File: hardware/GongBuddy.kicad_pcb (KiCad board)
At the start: 2 copper layers, 54 x 77 mm, 49 parts, among them J1 USB_B_Mini, J2 Conn_01x05, J3 2908-05WB-MG, J4 Conn_01x04, J5 Conn_01x02, J6 Conn_01x06, J7 Conn_Coaxial, J8 Conn_01x15, Q1 MMBT3904, U1 TPS7A19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

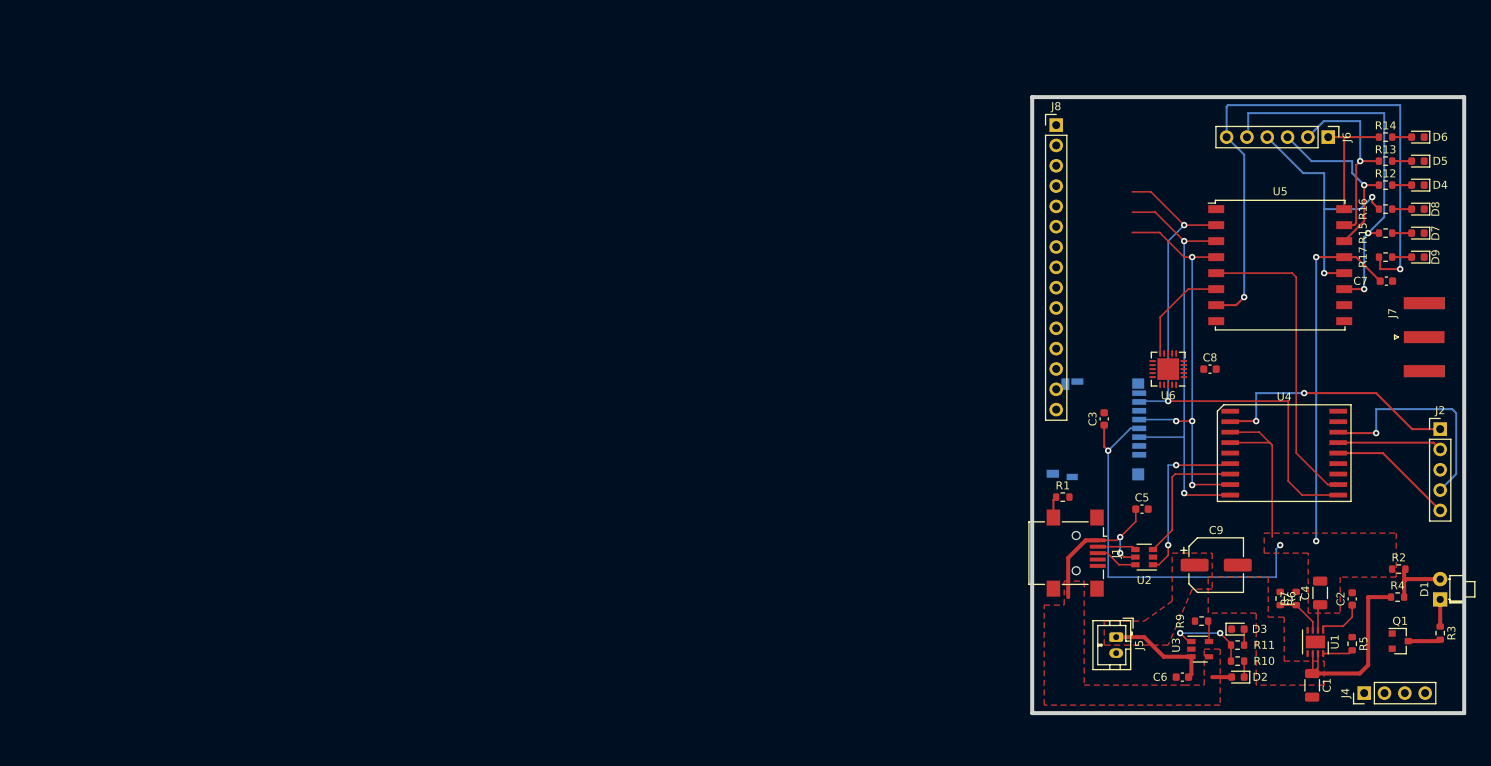
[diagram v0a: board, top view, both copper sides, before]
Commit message: Finished the layout and routing.
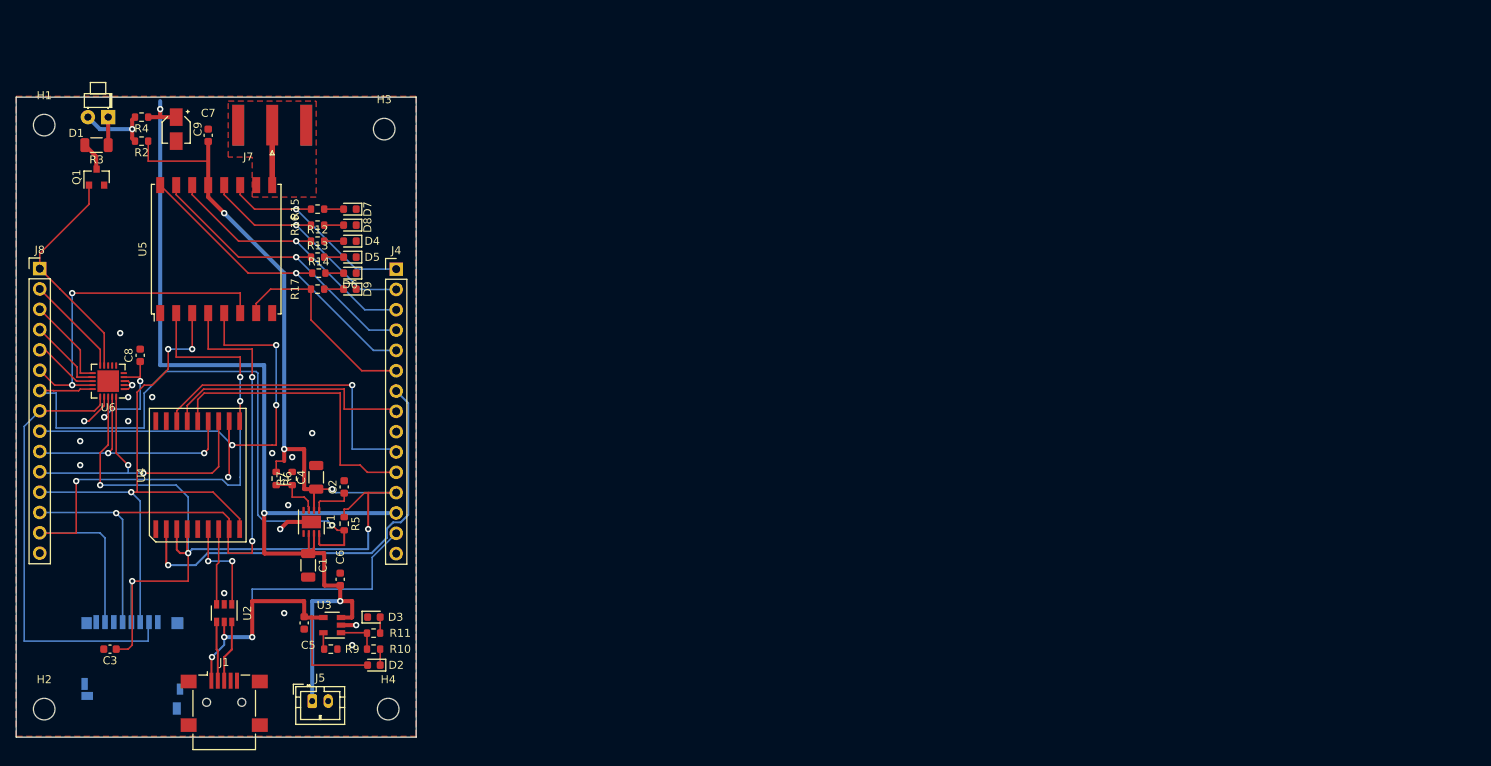
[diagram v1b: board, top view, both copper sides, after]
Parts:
- removed J2: Conn_01x05, Connector_PinHeader_2.54mm:PinHeader_1x05_P2.54mm_Vertical
- removed J6: Conn_01x06, Connector_PinHeader_2.54mm:PinHeader_1x06_P2.54mm_Vertical
- removed R1: 0, Resistor_SMD:R_0603_1608Metric
- added H1: MountingHole, MountingHole:MountingHole_2.7mm_M2.5, F.Cu at (33.5, 63.5)
- added H2: MountingHole, MountingHole:MountingHole_2.7mm_M2.5, F.Cu at (33.5, 136.5)
- added H3: MountingHole, MountingHole:MountingHole_2.7mm_M2.5, F.Cu at (76.0, 64.0)
- added H4: MountingHole, MountingHole:MountingHole_2.7mm_M2.5, F.Cu at (76.5, 136.5)
- C9: footprint Capacitor_SMD:CP_Elec_6.3x5.7 -> Capacitor_SMD:CP_Elec_3x5.3
- J4: value Conn_01x04 -> Conn_01x15; footprint Connector_PinHeader_2.54mm:PinHeader_1x04_P2.54mm_Vertical -> Connector_PinHeader_2.54mm:PinHeader_1x15_P2.54mm_Vertical
- R3: footprint Resistor_SMD:R_0603_1608Metric -> Resistor_SMD:R_1206_3216Metric
- moved R3 178.7 mm to (40.0, 66.0), turned to 180 degrees
- moved D1 177.1 mm to (41.5, 62.5), turned to 180 degrees
- moved Q1 173.0 mm to (40.0, 70.0), turned to 90 degrees
- moved R4 168.1 mm to (45.7, 62.5), turned to 180 degrees
- moved R2 166.0 mm to (45.7, 65.5), turned to 180 degrees
- moved C7 148.4 mm to (54.0, 64.8), turned to 90 degrees
- moved J7 146.4 mm to (62.0, 63.5), turned to 90 degrees
- moved C9 141.0 mm to (50.0, 64.0), turned to 270 degrees
- moved U4 135.8 mm to (52.7, 107.2), turned to 0 degrees
- moved D6 134.6 mm to (71.7, 82.0)
- moved R14 134.4 mm to (67.8, 82.0)
- moved D5 134.0 mm to (71.7, 80.0)
- moved R13 134.0 mm to (67.7, 80.0)
- moved C8 133.7 mm to (45.5, 92.3), turned to 90 degrees
- moved D4 133.7 mm to (71.7, 78.0)
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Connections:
- J1 pad 6: Net-(J1-Pad6) -> GND
- J4 pad 1: VCC -> /DIO3
- J4 pad 2: /VBAT -> /DIO4
- J4 pad 3: VBUS -> /DIO0
- J4 pad 4: GND -> /DIO1
- J8 pad 1: /SD_CS -> /BIG_LED
- J8 pad 10: /I2C_SDA -> /I2C_SCL
- J8 pad 11: /LORA_CS -> /I2C_SDA
- J8 pad 12: Net-(J8-Pad12) -> /SPI_MOSI
- J8 pad 14: /SPI_MOSI -> /SPI_MISO
- J8 pad 15: /SPI_MISO -> GND
- J8 pad 2: /LORA_RESET -> Net-(J8-Pad2)
- J8 pad 3: /BIG_LED -> Net-(J8-Pad3)
- J8 pad 4: /PG -> Net-(J8-Pad4)
- J8 pad 6: Net-(J8-Pad6) -> /LORA_RESET
- J8 pad 7: Net-(J8-Pad7) -> /PG
- J8 pad 8: Net-(J8-Pad8) -> /SD_CS
- J8 pad 9: /I2C_SCL -> /LORA_CS
- U6 pad 10: /LORA_RESET -> Net-(J8-Pad2)
- U6 pad 11: /BIG_LED -> Net-(J8-Pad3)
- U6 pad 12: /PG -> Net-(J8-Pad4)
- U6 pad 14: Net-(J8-Pad6) -> /LORA_RESET
- U6 pad 15: Net-(J8-Pad7) -> /PG
- U6 pad 16: Net-(J8-Pad8) -> /SD_CS
- U6 pad 9: /SD_CS -> /BIG_LED
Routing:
- net /VBAT: track 37.2 -> 132.3 mm, vias 0 -> 3
- net /PG: track 3.97 -> 79.7 mm, vias 0 -> 1
- net VCC: track 120.0 -> 195.4 mm, vias 4 -> 9
- net /SD_CS: track 0.00 -> 56.4 mm
- net /DIO5: track 75.0 -> 25.9 mm, vias 2 -> 0
- net VBUS: track 23.3 -> 69.0 mm, vias 2 -> 3
- net /I2C_SDA: track 0.00 -> 38.7 mm, vias 0 -> 2
- net /I2C_SCL: track 0.00 -> 32.1 mm, vias 0 -> 2
- net /LORA_RESET: track 13.0 -> 42.4 mm, vias 0 -> 2
- net /SPI_CLK: track 51.8 -> 80.9 mm, vias 4 -> 3
- net /BIG_LED: track 0.00 -> 28.4 mm
- net /DIO2: track 15.3 -> 40.1 mm, vias 0 -> 1
- net /LORA_CS: track 39.1 -> 63.5 mm, vias 0 -> 4
- net /VDD_OUT: track 31.6 -> 54.0 mm, vias 2 -> 1
- net /NRST: track 15.7 -> 37.2 mm
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- added copper zone on B.Cu, net GND
- added copper zone on F.Cu, net GND
- removed copper zone on F.Cu, net /VBAT
- removed copper zone on F.Cu, net VBUS
- removed copper zone on F.Cu, net VCC
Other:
- board size 54 x 77 mm -> 50 x 80 mm

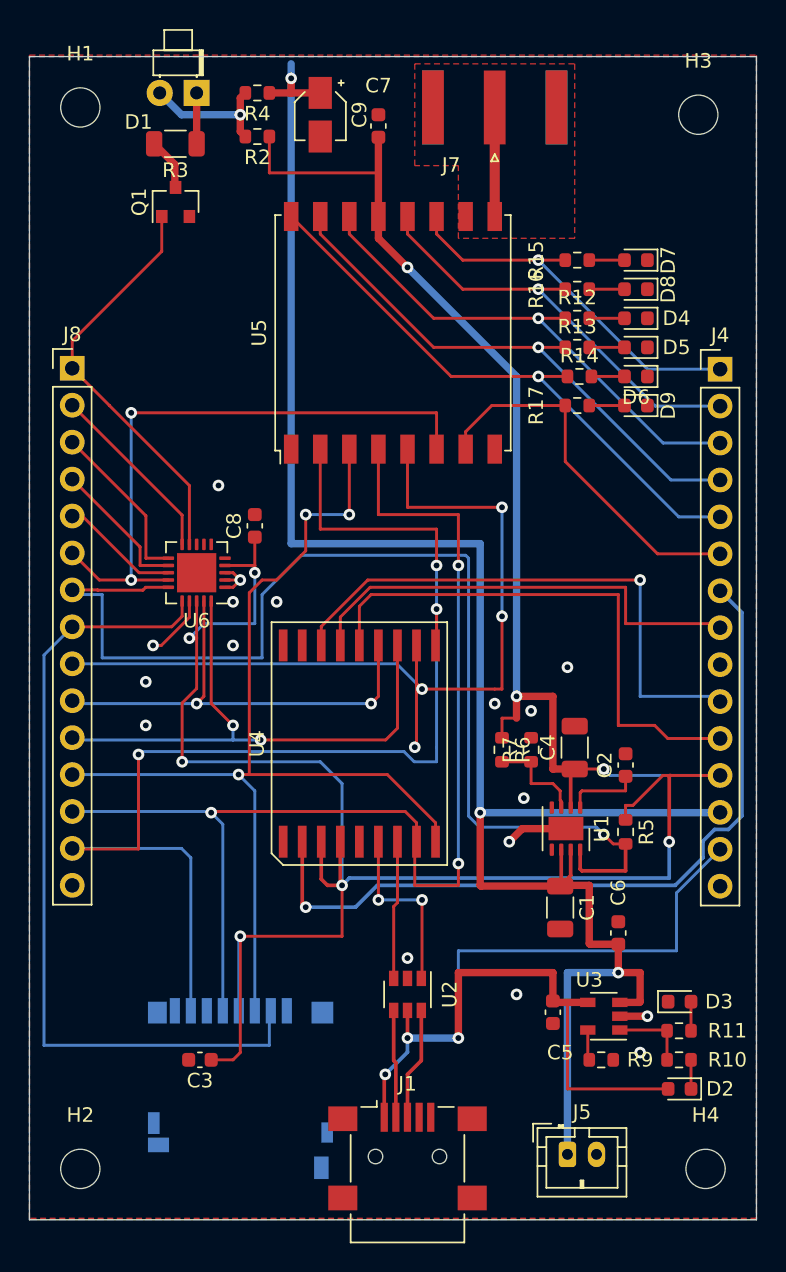
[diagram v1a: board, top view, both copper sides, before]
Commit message: Tweaked the layout slightly.
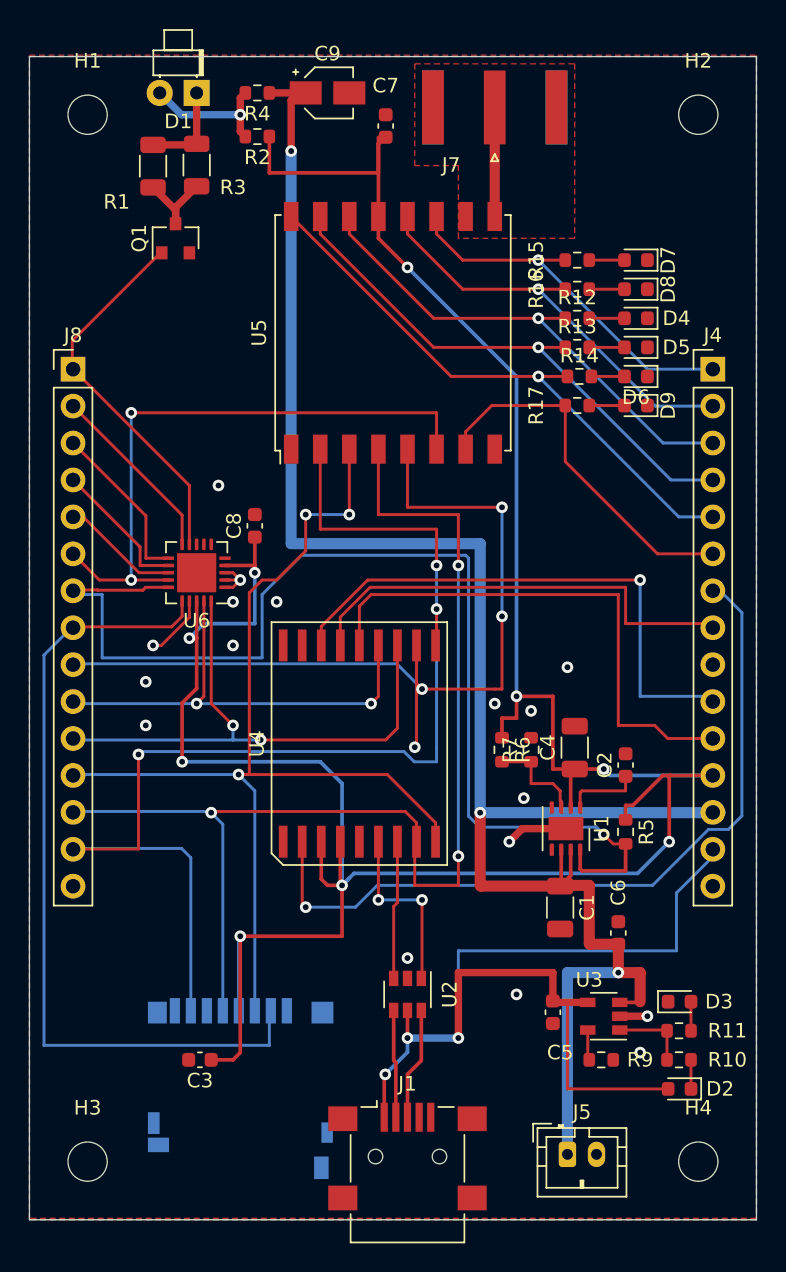
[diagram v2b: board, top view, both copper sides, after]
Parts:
- added R1: 50, Resistor_SMD:R_1206_3216Metric, F.Cu at (38.5, 67.5)
- moved H2 84.0 mm to (76.0, 64.0)
- moved H3 83.4 mm to (34.0, 136.0)
- moved Q1 2.50 mm to (40.0, 72.5)
- moved R3 2.07 mm to (41.5, 67.5), turned to 270 degrees
- moved C9 1.58 mm to (50.5, 62.5), turned to 0 degrees
- moved H1 0.71 mm to (34.0, 64.0)
- moved H4 0.71 mm to (76.0, 136.0)
- moved C7 0.50 mm to (54.5, 64.8)
- moved J4 0.50 mm to (77.0, 81.5)
- moved J8 0.08 mm to (33.0, 81.5)
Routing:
- net Net-(D1-Pad1): track 3.71 -> 6.74 mm
- net Net-(Q1-Pad3): track 3.61 -> 6.32 mm
- net /VBAT: track 132.3 -> 129.7 mm
- net /BIG_LED: track 28.4 -> 26.0 mm
- net /VDD_OUT: track 54.0 -> 53.3 mm
- net VCC: track 195.4 -> 194.9 mm
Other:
- board text added: "GongBuddy Rev A Copyright 2020 Nick Butts"

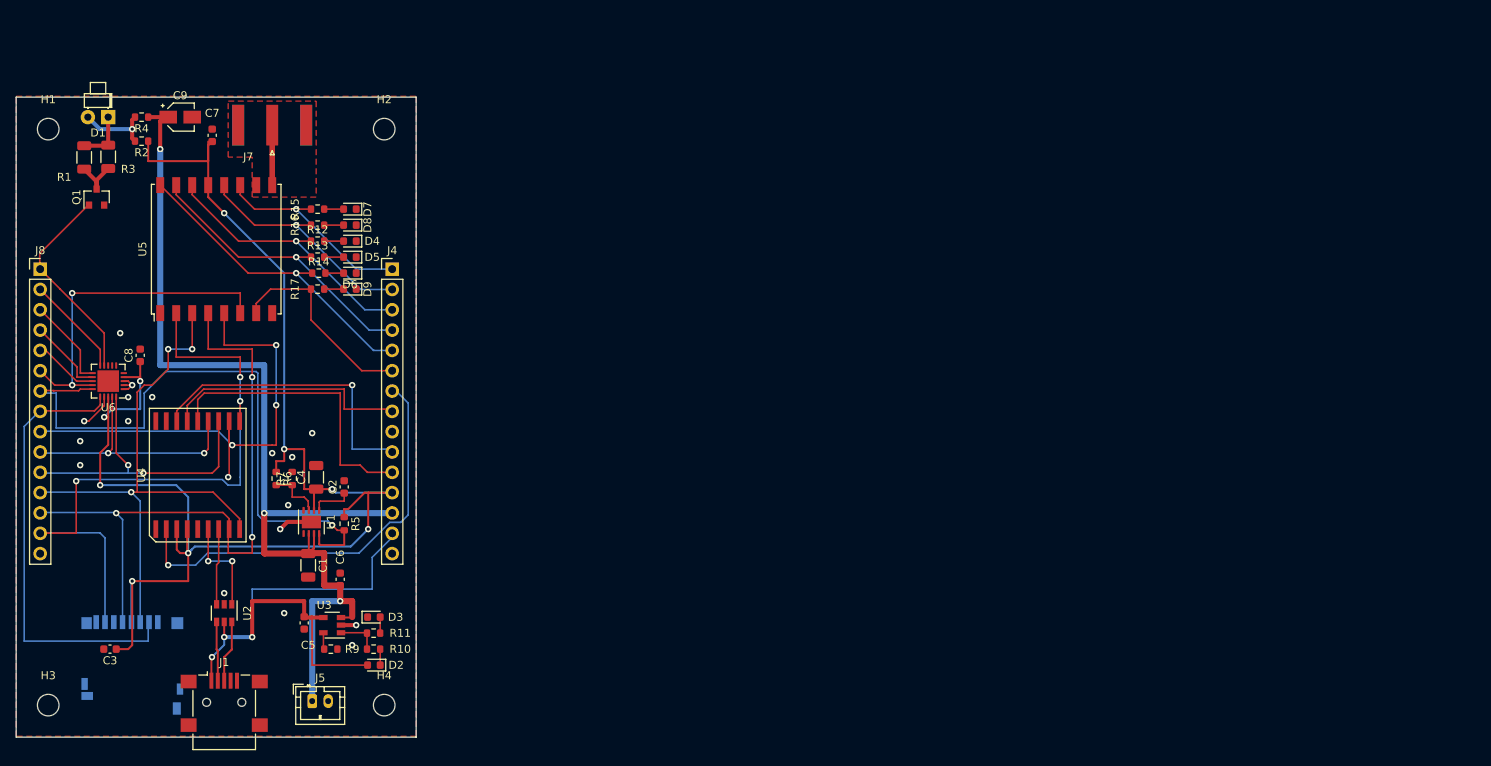
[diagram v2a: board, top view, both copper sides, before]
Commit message: Refactor board to a 4 layer.
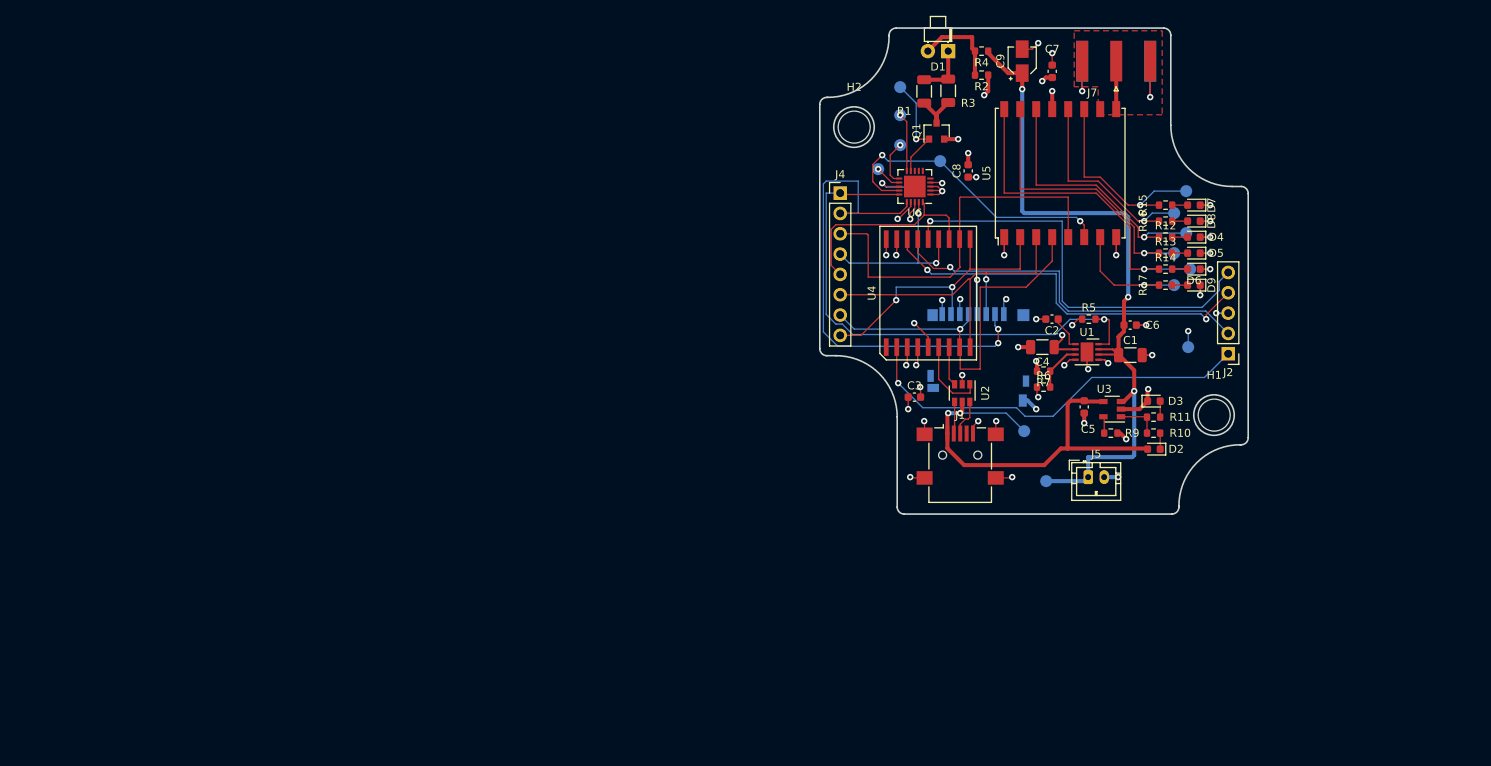
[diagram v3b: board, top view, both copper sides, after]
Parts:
- removed H3, H4: MountingHole, MountingHole:MountingHole_2.7mm_M2.5
- removed J8: Conn_01x15, Connector_PinHeader_2.54mm:PinHeader_1x15_P2.54mm_Vertical
- added J2: Conn_01x05, Connector_PinHeader_2.54mm:PinHeader_1x05_P2.54mm_Vertical, F.Cu at (181.5, 92.1)
- added TP1: TestPoint, TestPoint:TestPoint_Pad_D1.5mm, B.Cu at (176.2, 71.8)
- added TP10: TestPoint, TestPoint:TestPoint_Pad_D1.5mm, B.Cu at (140.5, 58.8)
- added TP11: TestPoint, TestPoint:TestPoint_Pad_D1.5mm, B.Cu at (140.5, 62.2)
- added TP12: TestPoint, TestPoint:TestPoint_Pad_D1.5mm, B.Cu at (140.5, 66.0)
- added TP13: TestPoint, TestPoint:TestPoint_Pad_D1.5mm, B.Cu at (137.8, 69.0)
- added TP14: TestPoint, TestPoint:TestPoint_Pad_D1.5mm, B.Cu at (142.2, 71.2)
- added TP15: TestPoint, TestPoint:TestPoint_Pad_D1.5mm, B.Cu at (145.5, 68.0)
- added TP2: TestPoint, TestPoint:TestPoint_Pad_D1.5mm, B.Cu at (174.8, 74.5)
- added TP3: TestPoint, TestPoint:TestPoint_Pad_D1.5mm, B.Cu at (176.2, 77.0)
- added TP4: TestPoint, TestPoint:TestPoint_Pad_D1.5mm, B.Cu at (174.8, 79.5)
- added TP5: TestPoint, TestPoint:TestPoint_Pad_D1.5mm, B.Cu at (176.8, 81.5)
- added TP6: TestPoint, TestPoint:TestPoint_Pad_D1.5mm, B.Cu at (174.8, 83.5)
- added TP7: TestPoint, TestPoint:TestPoint_Pad_D1.5mm, B.Cu at (176.5, 91.2)
- added TP8: TestPoint, TestPoint:TestPoint_Pad_D1.5mm, B.Cu at (158.8, 108.0)
- added TP9: TestPoint, TestPoint:TestPoint_Pad_D1.5mm, B.Cu at (156.0, 101.8)
- H1, H2: footprint MountingHole:MountingHole_2.7mm_M2.5 -> MountingHole:MountingHole_4mm
- J4: value Conn_01x15 -> Conn_01x08; footprint Connector_PinHeader_2.54mm:PinHeader_1x15_P2.54mm_Vertical -> Connector_PinHeader_2.54mm:PinHeader_1x08_P2.54mm_Vertical
- moved H1 150.1 mm to (179.8, 99.8)
- moved J3 112.5 mm to (150.2, 88.0)
- moved C1 106.1 mm to (169.3, 92.2), turned to 0 degrees
- moved C8 106.0 mm to (149.0, 69.2)
- moved R12 106.0 mm to (173.7, 77.5)
- moved R13 106.0 mm to (173.7, 79.5)
- moved R15 106.0 mm to (173.7, 73.5)
- moved R16 106.0 mm to (173.7, 75.5)
- moved R17 106.0 mm to (173.7, 83.5)
- moved U5 105.9 mm to (160.5, 69.5)
- moved R14 105.9 mm to (173.7, 81.5)
- moved J7 105.8 mm to (167.5, 55.5)
- moved D4 105.5 mm to (177.2, 77.5)
- moved D5 105.5 mm to (177.2, 79.5)
- moved D6 105.5 mm to (177.2, 81.5)
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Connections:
- J4 pad 1: /DIO3 -> /PG
- J4 pad 2: /DIO4 -> /SD_CS
- J4 pad 3: /DIO0 -> /LORA_CS
- J4 pad 4: /DIO1 -> /I2C_SCL
- J4 pad 5: /DIO2 -> /I2C_SDA
- J4 pad 6: /DIO5 -> /SPI_MOSI
- J4 pad 7: /VDD_OUT -> /SPI_CLK
- J4 pad 8: /SWD_CLK -> /SPI_MISO
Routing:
- net VCC: track 194.9 -> 31.2 mm, vias 9 -> 14
- net GND: track 14.2 -> 93.2 mm, vias 17 -> 43
- net /SPI_MISO: track 83.0 -> 38.1 mm, vias 3 -> 2
- net /VBAT: track 129.7 -> 89.1 mm
- net /SPI_CLK: track 80.9 -> 49.2 mm, vias 3 -> 1
- net /SPI_MOSI: track 71.9 -> 43.7 mm, vias 3 -> 1
- net VBUS: track 69.0 -> 53.4 mm, vias 3 -> 2
- net /SWD_CLK: track 31.5 -> 47.1 mm, vias 0 -> 1
- net /LORA_CS: track 63.5 -> 48.1 mm, vias 4 -> 0
- net /NRST: track 37.2 -> 52.4 mm, vias 0 -> 1
- net /I2C_SDA: track 38.7 -> 26.1 mm, vias 2 -> 0
- net /PG: track 79.7 -> 67.0 mm
- net /BIG_LED: track 26.0 -> 13.8 mm, vias 0 -> 1
- net /SWD_IO: track 38.2 -> 48.9 mm, vias 1 -> 2
- net /DIO5: track 25.9 -> 16.1 mm, vias 0 -> 1
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- added copper zone on In2.Cu, net GND
- added copper zone on In1.Cu, net VCC
- removed copper zone on B.Cu, net GND
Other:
- board size 50 x 80 mm -> 53.6 x 60.8 mm
- copper layers 2 -> 4
- rule trace_min: 0.2 -> 0.1524
- board text added: "GongBuddy Rev B Copyright 2020 Nick Butts"
- board text removed: "GongBuddy Rev A Copyright 2020 Nick Butts"
